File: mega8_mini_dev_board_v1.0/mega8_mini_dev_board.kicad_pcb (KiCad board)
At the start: 2 copper layers, 113.6 x 127 mm, 38 parts, among them J1 Barrel_Jack_Switch, J10 Conn_01x01_Female, J2 AVR-ISP-6, J3 Conn_01x14_Female, J4 Conn_01x14_Female, J5 Conn_01x04_Female, J6 Conn_01x04_Female, J7 Conn_01x04_Female, J8 Conn_01x02_Female, J9 Conn_01x02_Female, SW1 SW_Push, SW2 SW_Push, SW3 SW_Push, U1 L7805, U2 AP1117-33, U3 ATmega8A-PU, Y1 Crystal

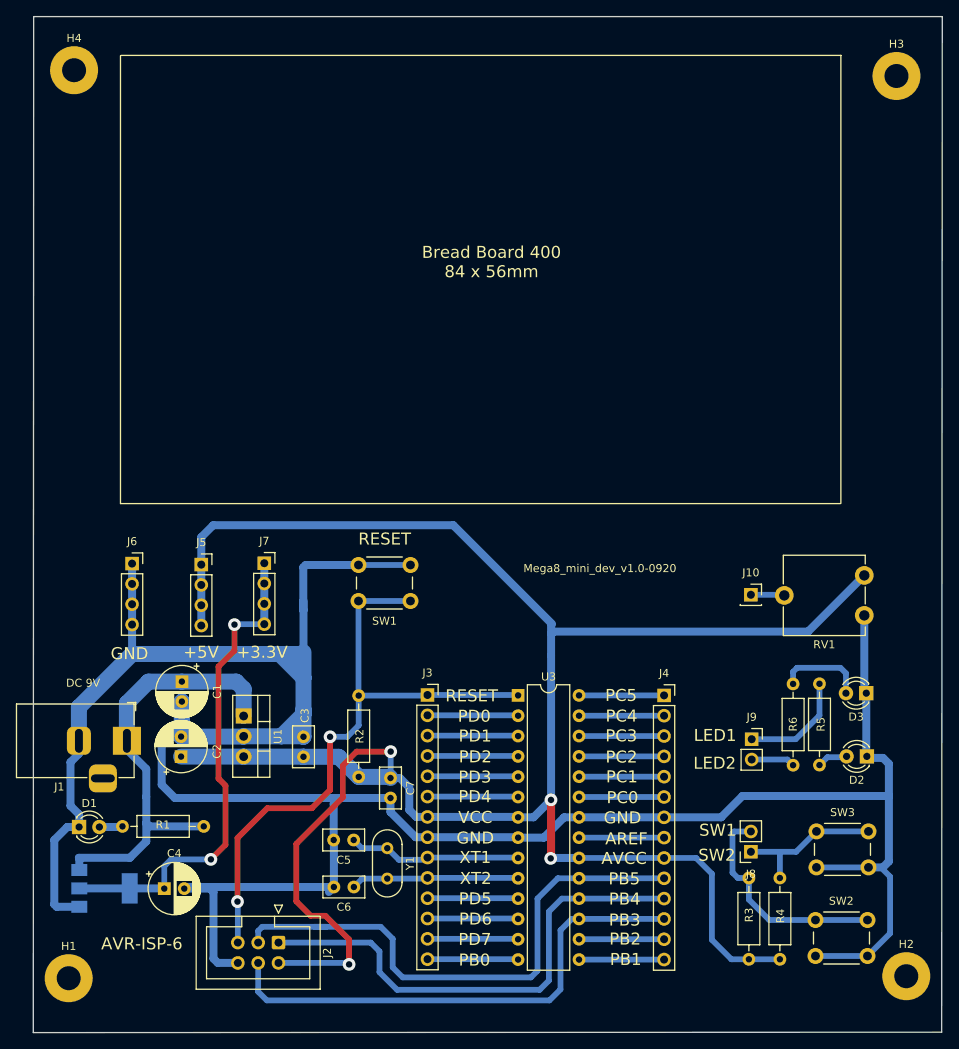
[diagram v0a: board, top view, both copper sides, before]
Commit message: Some pad size chaged
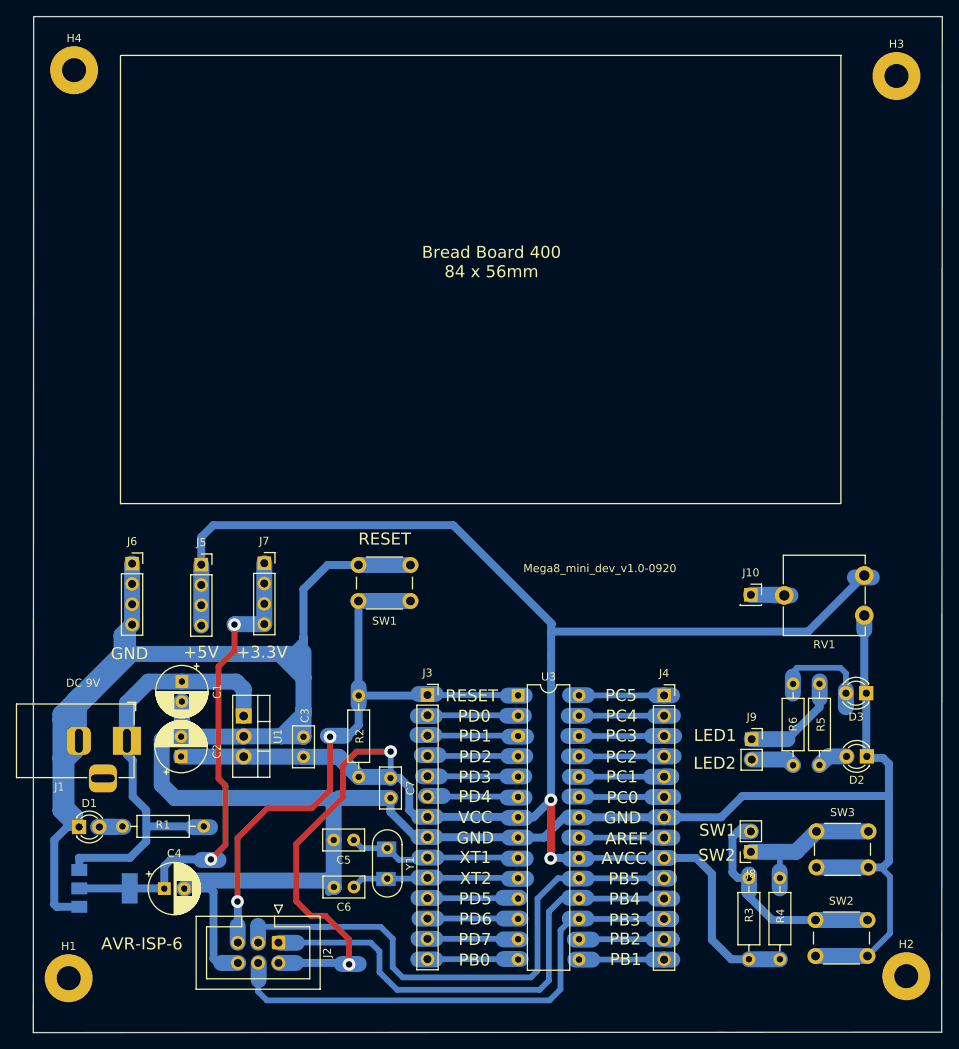
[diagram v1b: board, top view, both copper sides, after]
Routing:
- net GND: track 358.1 -> 433.5 mm
- net +5V: track 273.1 -> 297.5 mm
- net RESET: track 80.0 -> 90.6 mm
- net +3V3: track 62.3 -> 72.0 mm
- net Net-(J8-Pad1): track 19.1 -> 26.9 mm
- net /PB3: track 63.3 -> 69.4 mm
- net /PB5: track 69.0 -> 74.5 mm
- net /PB4: track 61.9 -> 67.2 mm
- net Net-(J9-Pad1): track 13.7 -> 18.1 mm
- net Net-(D1-Pad2): track 2.92 -> 7.17 mm
- net /PD4: track 11.3 -> 15.6 mm
- net /PD2: track 11.3 -> 15.6 mm
- net /PD0: track 11.3 -> 15.6 mm
- net Net-(D3-Pad2): track 11.1 -> 15.4 mm
- net /XTAL2: track 21.0 -> 25.3 mm
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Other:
- rule pad_to_mask_clearance: 0.05 -> 0.8
